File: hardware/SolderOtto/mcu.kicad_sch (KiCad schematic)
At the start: 9 parts, among them J301 TC-2050, U301 STM32L496RGTx, Y301 Crystal

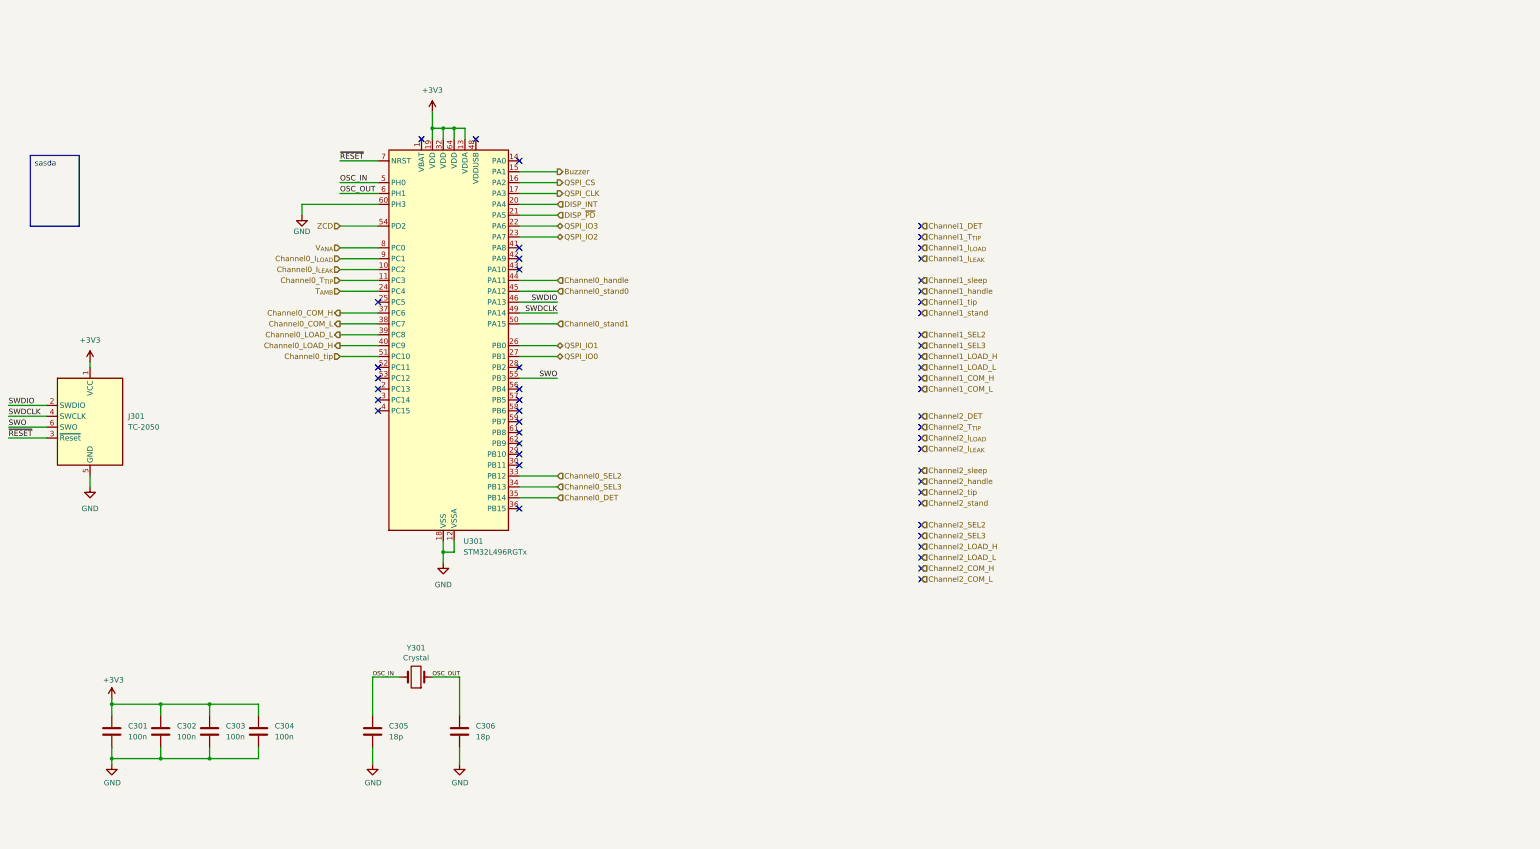
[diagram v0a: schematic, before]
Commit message: add support for tweezers AM-120
change mcu to stm32h573VI
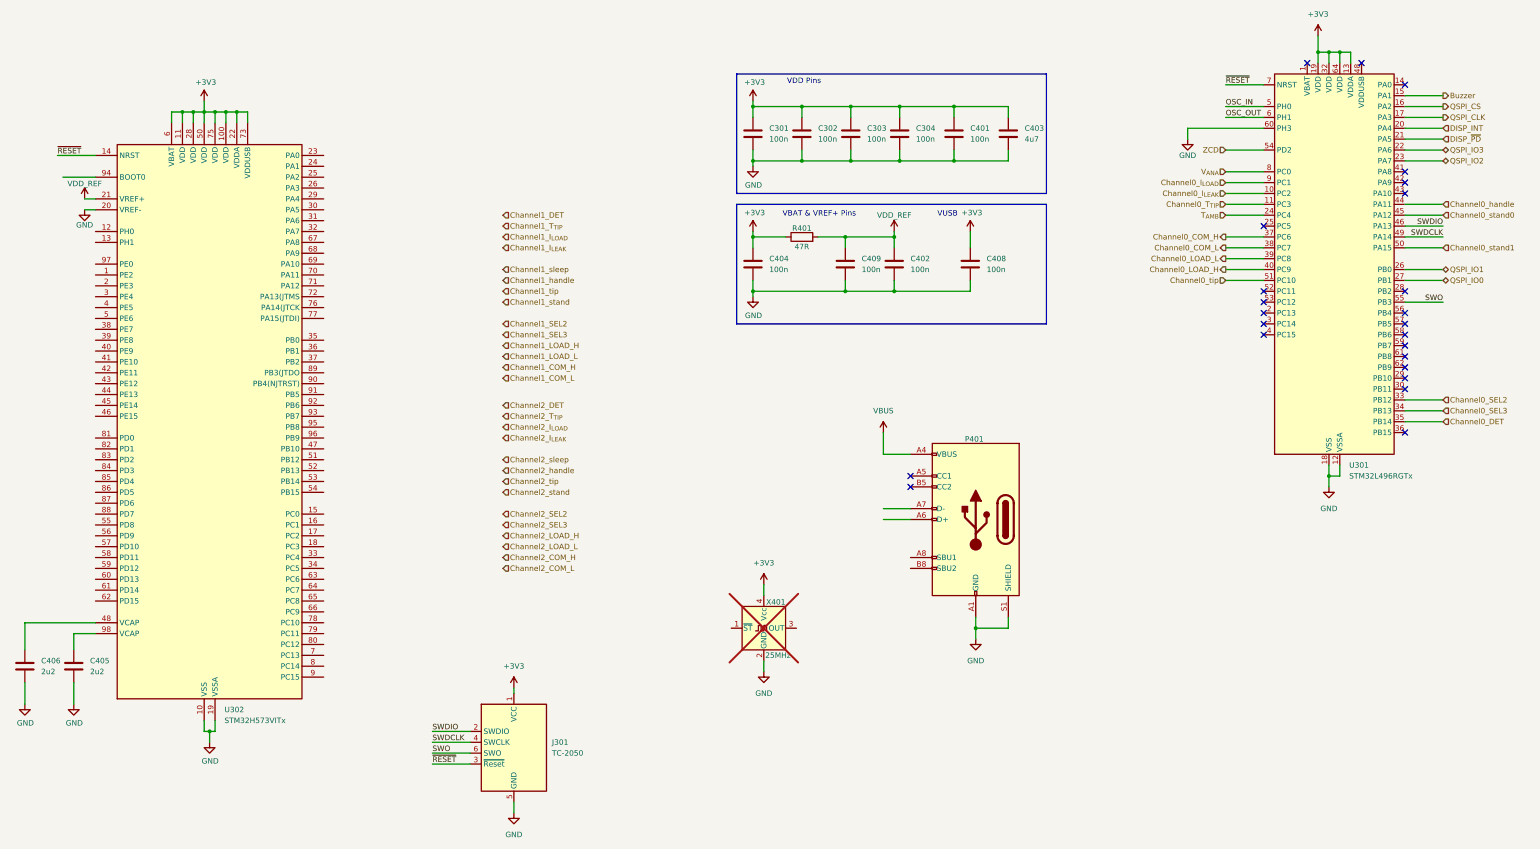
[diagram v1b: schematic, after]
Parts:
- removed C305, C306: 18p, Capacitor_SMD:C_0603_1608Metric, symbol Device:C
- removed Y301: Crystal, Crystal:Crystal_SMD_0603-2Pin_6.0x3.5mm, symbol Device:Crystal
- added C401, C402, C404, C408, C409: 100n, Capacitor_SMD:C_0603_1608Metric, symbol Device:C
- added C403: 4u7, Capacitor_SMD:C_0603_1608Metric, symbol Device:C
- added C405, C406: 2u2, Capacitor_SMD:C_0603_1608Metric, symbol Device:C
- added P401: USB_C_Plug_USB2.0, symbol mylib_connectors:USB_C_Plug_USB2.0
- added R401: 47R, symbol Device:R
- added U302: STM32H573VITx, Package_QFP:LQFP-100_14x14mm_P0.5mm, symbol MCU_ST_STM32H5:STM32H573VITx
- added X401: 25MHz, Oscillator:Oscillator_SMD_SeikoEpson_SG210-4Pin_2.5x2.0mm, symbol Oscillator:SG-210STF
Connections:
- net +3V3: now also C401.1, C403.1, C404.1, C408.1, R401.1, U302.100 (VDD), U302.11 (VDD), U302.22 (VDDA), U302.28 (VDD), U302.50 (VDD), U302.6 (VBAT), U302.73 (VDDUSB), U302.75 (VDD), X401.4 (Vcc)
- net GND: now also C401.2, C402.2, C403.2, C404.2, C405.2, C406.2, C408.2, C409.2, P401.A1 (GND), P401.A12 (GND), P401.B1 (GND), P401.B12 (GND), P401.S1 (SHIELD), U302.10 (VSS), U302.19 (VSSA), U302.20 (VREF-), U302.27 (VSS), U302.49 (VSS), U302.74 (VSS), U302.99 (VSS), X401.2 (GND)
- net ~{RESET}: now also U302.14 (NRST)
- new net: C405.1, U302.98 (VCAP)
- new net: C406.1, U302.48 (VCAP)
- new net: P401.A6 (D+), P401.B6 (D+)
- new net: P401.A7 (D-), P401.B7 (D-)
- new net VBUS: P401.A4 (VBUS), P401.A9 (VBUS), P401.B4 (VBUS), P401.B9 (VBUS)
- new net VDD_REF: C402.1, C409.1, R401.2, U302.21 (VREF+)
- no-connect marks 50 -> 24
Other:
- note added: "VBAT & VREF+ Pins"
- note added: "VDD Pins"
- note added: "VUSB"
- moved on the sheet: C301, C302, C303, C304, J301, U301

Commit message: save wip
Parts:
- P401: footprint (none) -> mylib_connector:USB_C_Receptacle_Molex_C_24P_SMD_RA
- R401: footprint (none) -> Resistor_SMD:R_0603_1608Metric

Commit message: wip
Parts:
- removed C402, C408, C409: 100n, Capacitor_SMD:C_0603_1608Metric, symbol Device:C
- removed C405, C406: 2u2, Capacitor_SMD:C_0603_1608Metric, symbol Device:C
- removed R401: 47R, Resistor_SMD:R_0603_1608Metric, symbol Device:R
- removed U302: STM32H573VITx, Package_QFP:LQFP-100_14x14mm_P0.5mm, symbol MCU_ST_STM32H5:STM32H573VITx
- removed X401: 25MHz, Oscillator:Oscillator_SMD_SeikoEpson_SG210-4Pin_2.5x2.0mm, symbol Oscillator:SG-210STF
- added C305: 10n, Capacitor_SMD:C_0603_1608Metric, symbol Device:C
- added C306, C307: 1u, Capacitor_SMD:C_0603_1608Metric, symbol Device:C
- added C308, C309: 100n, Capacitor_SMD:C_0603_1608Metric, symbol Device:C
- added C310, C311: 9p, Capacitor_SMD:C_0603_1608Metric, symbol Device:C
- added L301, L302: 600R@100MHz, Inductor_SMD:L_0603_1608Metric, symbol Device:L
- added U302: STM32G474VETx, Package_QFP:LQFP-100_14x14mm_P0.5mm, symbol MCU_ST_STM32G4:STM32G474VETx
- added Y301: 32.768 kHz, Crystal:Crystal_SMD_MicroCrystal_CC8V-T1A-2Pin_2.0x1.2mm, symbol Device:Crystal
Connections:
- net +3V3: now also L301.1, U302.100 (VDD), U302.24 (VDD), U302.49 (VDD), U302.64 (VDD), U302.75 (VDD)
- net Buzzer: no longer U301.15 (PA1)
- net Channel0_DET: no longer U301.35 (PB14)
- net Channel0_I_{LEAK}: no longer U301.10 (PC2)
- net Channel0_I_{LOAD}: no longer U301.9 (PC1)
- net Channel0_SEL2: no longer U301.33 (PB12)
- net Channel0_SEL3: no longer U301.34 (PB13)
- net Channel0_T_{TIP}: no longer U301.11 (PC3)
- net Channel0_handle: no longer U301.44 (PA11)
- net Channel0_tip: no longer U301.51 (PC10)
- net GND: now also C305.1, C306.2, C307.2, C308.2, C309.2, C310.2, C311.2, U302.23 (VSS), U302.35 (VSSA), U302.48 (VSS), U302.63 (VSS), U302.74 (VSS), U302.99 (VSS)
- net T_{AMB}: no longer U301.24 (PC4)
- net VDD_REF: now also C307.1, C308.1, L302.2, U302.36 (VREF+)
- net V_{ANA}: no longer U301.8 (PC0)
- net ZCD: no longer U301.54 (PD2)
- net Channel0_COM_H: no longer names the net of U301.37 (PC6)
- net Channel0_COM_L: no longer names the net of U301.38 (PC7)
- net Channel0_LOAD_H: no longer names the net of U301.40 (PC9)
- net Channel0_LOAD_L: no longer names the net of U301.39 (PC8)
- net Channel0_stand0: no longer names the net of U301.45 (PA12)
- net Channel0_stand1: no longer names the net of U301.50 (PA15)
- net DISP_INT: no longer names the net of U301.20 (PA4)
- net DISP_~{PD}: no longer names the net of U301.21 (PA5)
- net QSPI_CLK: no longer names the net of U301.17 (PA3)
- net QSPI_CS: no longer names the net of U301.16 (PA2)
- net QSPI_IO0: no longer names the net of U301.27 (PB1)
- net QSPI_IO1: no longer names the net of U301.26 (PB0)
- net QSPI_IO2: no longer names the net of U301.23 (PA7)
- net QSPI_IO3: no longer names the net of U301.22 (PA6)
- new net: C311.1, U302.8 (PC14), Y301.2
- new net: C310.1, U302.9 (PC15), Y301.1
- new net VBAT: C309.1, U302.6 (VBAT)
- new net VDDA: C305.2, C306.1, L301.2, L302.1, U302.37 (VDDA)
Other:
- note removed: "VUSB"
- moved on the sheet: C301, C302, C303, C304, C401, C403, C404, J301, P401, U301

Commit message: save wip
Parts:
- removed C401, C404: 100n, Capacitor_SMD:C_0603_1608Metric, symbol Device:C
- removed J301: TC-2050, mylib_connector:TC-2030, symbol mylib_connectors:TC-2030
- removed L301: 600R@100MHz, Inductor_SMD:L_0603_1608Metric, symbol Device:L
- removed U301: STM32L496RGTx, Package_QFP:LQFP-64_10x10mm_P0.5mm, symbol MCU_ST_STM32L4:STM32L496RGTx
- removed U302: STM32G474VETx, Package_QFP:LQFP-100_14x14mm_P0.5mm, symbol MCU_ST_STM32G4:STM32G474VETx
- added C312, C314, C315, C316: 100n, Resistor_SMD:R_0402_1005Metric, symbol Device:C
- added C313: 1u, Resistor_SMD:R_0402_1005Metric, symbol Device:C
- added J302: TC-2050, mylib_connector:TC-2050, symbol mylib_connectors:TC-2050
- added R301, R302: 0, Resistor_SMD:R_0603_1608Metric, symbol Device:R
- added SW302: SW_Push, Button_Switch_SMD:SW_Push_SPST_NO_Alps_SKRK, symbol Switch:SW_Push
- added U301: USBLC6-2SC6, Package_TO_SOT_SMD:SOT-23-6, symbol Power_Protection:USBLC6-2SC6
- added U303: MX25R3235FM1xx0, Package_SO:SOP-8_3.9x4.9mm_P1.27mm, symbol Memory_Flash:MX25R3235FM1xx0
- added U304: STM32G474QETx, Package_QFP:LQFP-128_14x14mm_P0.4mm, symbol MCU_ST_STM32G4:STM32G474QETx
- C301, C302, C303, C304, C308, C309: footprint Capacitor_SMD:C_0603_1608Metric -> Resistor_SMD:R_0402_1005Metric; Digikey 1276-1000-1-ND -> 478-KGM05AR71C104KHCT-ND
- C305: footprint Capacitor_SMD:C_0603_1608Metric -> Resistor_SMD:R_0402_1005Metric; Digikey 399-C0603C103K3RAC7867CT-ND -> 1276-1028-1-ND
- C306: footprint Capacitor_SMD:C_0603_1608Metric -> Resistor_SMD:R_0402_1005Metric; Digikey 1276-1184-1-ND -> 1276-1067-1-ND
- C307: value 1u -> 100n; footprint Capacitor_SMD:C_0603_1608Metric -> Resistor_SMD:R_0402_1005Metric; Digikey 1276-1184-1-ND -> 478-KGM05AR71C104KHCT-ND
- C403: footprint Capacitor_SMD:C_0603_1608Metric -> Resistor_SMD:R_0402_1005Metric; Digikey 445-9050-1-ND -> 490-GRM155C61E475ME15DCT-ND
- L302: footprint Inductor_SMD:L_0603_1608Metric -> Inductor_SMD:L_0402_1005Metric; Digikey 490-1014-1-ND -> 490-1006-1-ND
- Y301: Digikey 535-10246-1-ND -> 2195-CM8V-T1A-32.768KHZ-9PF-20PPM-TA-QCCT-ND
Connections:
- net +3V3: now also C307.1, C308.1, C309.1, L302.1, C314.1, C315.1, C316.1, J302.1 (VCC), U303.8 (VCC), U304.111 (VDD), U304.128 (VDD), U304.13 (VDD), U304.31 (VDD), U304.47 (VDD), U304.64 (VDD), U304.79 (VDD), U304.95 (VDD); no longer C302.1, C303.1
- net Buzzer: now also U304.7 (PC13)
- net Channel0_COM_SW: now also U304.29 (PA2)
- net Channel0_DET: now also U304.109 (PD1)
- net Channel0_I_{LEAK}: now also U304.24 (PC2)
- net Channel0_I_{LOAD}: now also U304.25 (PC3)
- net Channel0_LOAD0_SW: now also U304.27 (PA0)
- net Channel0_LOAD1_SW: now also U304.28 (PA1)
- net Channel0_LOW_SIDE_SW: now also U304.26 (PF2)
- net Channel0_SEL1: now also U304.16 (PF8)
- net Channel0_SEL2: now also U304.17 (PF9)
- net Channel0_SEL3: now also U304.18 (PF10)
- net Channel0_T_{TIP}: now also U304.23 (PC1)
- net Channel0_handle: now also U304.22 (PC0)
- net Channel0_iron: now also U304.108 (PD0)
- net Channel0_stand: now also U304.66 (PB12)
- net Channel0_tip: now also U304.103 (PG5)
- net Channel1_COM_SW: now also U304.41 (PB2)
- net Channel1_DET: now also U304.107 (PG9)
- net Channel1_I_{LEAK}: now also U304.35 (PA6)
- net Channel1_I_{LOAD}: now also U304.36 (PA7)
- net Channel1_LOAD0_SW: now also U304.39 (PB0)
- net Channel1_LOAD1_SW: now also U304.40 (PB1)
- net Channel1_LOW_SIDE_SW: now also U304.38 (PC5)
- net Channel1_SEL1: now also U304.48 (PF11)
- net Channel1_SEL2: now also U304.49 (PF12)
- net Channel1_SEL3: now also U304.50 (PF13)
- net Channel1_T_{TIP}: now also U304.34 (PA5)
- net Channel1_handle: now also U304.33 (PA4)
- net Channel1_iron: now also U304.119 (PB4)
- net Channel1_stand: now also U304.67 (PB13)
- net Channel1_tip: now also U304.104 (PG6)
- net Channel2_COM_SW: now also U304.77 (PD15)
- net Channel2_DET: now also U304.121 (PB6)
- net Channel2_I_{LEAK}: now also U304.53 (PE7)
- net Channel2_I_{LOAD}: now also U304.72 (PD10)
- net Channel2_LOAD0_SW: now also U304.80 (PC6)
- net Channel2_LOAD1_SW: now also U304.81 (PC7)
- net Channel2_LOW_SIDE_SW: now also U304.82 (PG0)
- net Channel2_SEL1: now also U304.62 (PB10)
- net Channel2_SEL2: now also U304.65 (PB11)
- net Channel2_SEL3: now also U304.52 (PF15)
- net Channel2_T_{TIP}: now also U304.54 (PE8)
- net Channel2_handle: now also U304.55 (PE9)
- net Channel2_iron: now also U304.120 (PB5)
- net Channel2_stand: now also U304.68 (PB14)
- net Channel2_tip: now also U304.105 (PG7)
- net Channel3_COM_SW: now also U304.86 (PG4)
- net Channel3_DET: now also U304.124 (PB9)
- net Channel3_I_{LEAK}: now also U304.74 (PD12)
- net Channel3_I_{LOAD}: now also U304.73 (PD11)
- net Channel3_LOAD0_SW: now also U304.87 (PC8)
- net Channel3_LOAD1_SW: now also U304.88 (PC9)
- net Channel3_LOW_SIDE_SW: now also U304.89 (PA8)
- net Channel3_SEL1: now also U304.83 (PG1)
- net Channel3_SEL2: now also U304.84 (PG2)
- net Channel3_SEL3: now also U304.85 (PG3)
- net Channel3_T_{TIP}: now also U304.75 (PD13)
- net Channel3_handle: now also U304.76 (PD14)
- net Channel3_iron: now also U304.122 (PB7)
- net Channel3_stand: now also U304.69 (PB15)
- net Channel3_tip: now also U304.106 (PG8)
- net GND: now also C312.2, C313.2, C314.2, C315.2, C316.2, J302.3 (GND), J302.5 (GND), SW302.1, U301.2 (GND), U303.4 (GND), U304.110 (VSS), U304.12 (VSS), U304.123 (PB8), U304.127 (VSS), U304.30 (VSS), U304.42 (VSSA), U304.46 (VSS), U304.63 (VSS), U304.78 (VSS), U304.94 (VSS)
- net SWDCLK: now also J302.4 (TCK), U304.98 (PA14)
- net SWDIO: now also J302.2 (TMS), U304.96 (PA13)
- net SWO: now also J302.6 (TDO), U304.118 (PB3)
- net T_{AMB}: now also U304.70 (PD8)
- net VBAT: now also C303.1, U304.6 (VBAT); no longer C309.1
- net VBUS: now also U301.5 (VBUS)
- net VDDA: now also L302.2, C312.1, C313.1, U304.43 (VREF+), U304.44 (VREF_+), U304.45 (VDDA); no longer L302.1
- net V_{ANA}: now also U304.71 (PD9)
- net ZCD: now also U304.125 (PE0)
- net ~{RESET}: now also C302.1, J302.10 (RESET), SW302.2, U304.21 (PG10)
- net LSE_IN: now reaches C311.1, Y301.2
- net LSE_IN: now also U304.8 (PC14)
- net LSE_OUT: now reaches C310.1, Y301.1
- net LSE_OUT: now also U304.9 (PC15)
- net at P401.A5 (CC1): now also R301.2
- net _D+: now reaches P401.A6 (D+), P401.B6 (D+)
- net _D+: now also U301.3 (I/O2)
- net _D-: now reaches P401.A7 (D-), P401.B7 (D-)
- net _D-: now also U301.1 (I/O1)
- net at P401.B5 (CC2): now also R302.2
- removed net VDD_REF: C307.1, C308.1, L302.2
- new net D+: U301.4 (I/O2), U304.93 (PA12)
- new net D-: U301.6 (I/O1), U304.92 (PA11)
- new net DBG_RX: J302.7 (RTCLK), R302.1, U304.91 (PA10)
- new net DBG_TX: J302.8 (TDI), R301.1, U304.90 (PA9)
- new net DISP_CLK: U304.1 (PE2)
- new net DISP_INT: U304.126 (PE1)
- new net DISP_MISO: U304.4 (PE5)
- new net DISP_MOSI: U304.5 (PE6)
- new net DISP_NSS: U304.3 (PE4)
- new net DISP_~{PD}: U304.2 (PE3)
- new net EXT_0: U304.112 (PD2)
- new net EXT_1: U304.113 (PD3)
- new net EXT_2: U304.114 (PD4)
- new net EXT_3: U304.115 (PD5)
- new net EXT_4: U304.116 (PD6)
- new net EXT_5: U304.117 (PD7)
- new net QSPI_CLK: U303.1 (~{CS}), U304.56 (PE10)
- new net QSPI_IO0: U303.5 (SI/SIO0), U304.58 (PE12)
- new net QSPI_IO1: U303.2 (SO/SIO1), U304.59 (PE13)
- new net QSPI_IO2: U303.3 (~{WP}/SIO2), U304.60 (PE14)
- new net QSPI_IO3: U303.7 (~{RESET}/SIO3), U304.61 (PE15)
- new net QSPI_NCS: U303.6 (SCLK), U304.57 (PE11)
- no-connect marks 24 -> 17
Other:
- moved on the sheet: C301, C305, C306, C310, C311, L302, P401, Y301
